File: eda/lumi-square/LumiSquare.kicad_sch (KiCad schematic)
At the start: 70 parts, among them J1 Conn_01x02, J2 Conn_01x02, J3 Conn_01x02, J4 Conn_01x02, J5 USB_C_Receptacle_USB2.0, J6 Conn_01x04, J7 Conn_01x04, J8 Conn_01x04, J9 Conn_01x04, Q1 Q_PMOS_GSD, Q2 Q_PMOS_GSD, Q3 Q_PMOS_GSD, Q4 Q_PMOS_GSD, Q5 MMBT3904, Q6 MMBT3904, Q7 MMBT3904, Q8 MMBT3904, U1 MCP2200-I-SO, U2 ATmega1284-A, U3 ATtiny861A-S, U4 STP16CPC05MTR, U5 TPS3840, U6 TPS3840

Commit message: - Connected power portion of the schmatic - added components to the pcb editor
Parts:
- removed C1, C2, C3, C4: C_Polarized_US, Capacitor_SMD:CP_Elec_5x5.3, symbol Device:C_Polarized_US
- removed C10, C15, C16, C17, C18, C19, C20, C21, C5, C6, C7, C8, C9: C, Capacitor_SMD:C_0805_2012Metric_Pad1.18x1.45mm_HandSolder, symbol Device:C
- removed J1, J2, J3, J4: Conn_01x02, Connector_PinSocket_2.54mm:PinSocket_1x02_P2.54mm_Vertical, symbol Connector_Generic:Conn_01x02
- removed J5: USB_C_Receptacle_USB2.0, Connector_USB:USB_C_Receptacle_G-Switch_GT-USB-7010ASV, symbol Connector:USB_C_Receptacle_USB2.0
- removed Q1, Q2, Q3, Q4: Q_PMOS_GSD, Package_TO_SOT_SMD:SOT-23, symbol Device:Q_PMOS_GSD
- removed Q8: MMBT3904, Package_TO_SOT_SMD:SOT-23, symbol Transistor_BJT:MMBT3904
- removed R1, R10, R11, R12, R13, R14, R15, R16, R17, R18, R19, R2, R20, R21, R22, R23, R24, R25, R3, R4, R5, R6, R7, R8, R9: R, Resistor_SMD:R_0805_2012Metric, symbol Device:R
- removed U1: MCP2200-I-SO, Package_SO:SOIC-20W_7.5x12.8mm_P1.27mm, symbol Interface_USB:MCP2200-I-SO
- removed U2: ATmega1284-A, Package_QFP:TQFP-44_10x10mm_P0.8mm, symbol MCU_Microchip_ATmega:ATmega1284-A
- removed U5, U6: TPS3840, Package_TO_SOT_SMD:SOT-23-5, symbol Power_Supervisor_Custom:TPS3840
- added BT1: 4.2V Lipo, Connector_JST:JST_PH_S2B-PH-SM4-TB_1x02-1MP_P2.00mm_Horizontal, symbol Device:Battery_Cell
- added C1, C2: 4.7uF, Capacitor_SMD:C_0603_1608Metric_Pad1.08x0.95mm_HandSolder, symbol Device:C
- added C10, C8, C9: 100uF, Capacitor_THT:CP_Radial_D6.3mm_P2.50mm, symbol Device:C_Polarized
- added C23234545, C3: 1uF, Capacitor_SMD:C_0603_1608Metric_Pad1.08x0.95mm_HandSolder, symbol Device:C
- added C3245345: 2.2uF, Capacitor_SMD:C_0603_1608Metric_Pad1.08x0.95mm_HandSolder, symbol Device:C
- added C4, C6: 10uF, Capacitor_SMD:C_1206_3216Metric, symbol Device:C_Small
- added C5, C7: 22uF, Capacitor_SMD:C_1206_3216Metric, symbol Device:C_Small
- added D1: LED, LED_SMD:LED_1206_3216Metric, symbol Device:LED
- added D2, D3: 1N5819HW-7-F, Diode_SMD:D_SOD-123, symbol Diode:1N5819WS
- added D4: 1N4148W, Diode_SMD:D_SOD-123, symbol Diode:1N4148W
- added J1: USB_C_Receptacle_USB2.0_14P, Connector_USB:USB_C_Receptacle_G-Switch_GT-USB-7010ASV, symbol Connector:USB_C_Receptacle_USB2.0_14P
- added J6, J7: Conn_01x04, Connector_PinSocket_2.54mm:PinSocket_1x04_P2.54mm_Vertical, symbol Connector_Generic:Conn_01x04
- added L1, L2: 4.7uH, InductorCustom:Bourns SRP30xx, symbol Device:L
- added Q1: IRLML6244, Package_TO_SOT_SMD:SOT-23, symbol Transistor_FET:IRLML6244
- added Q2, Q4: MMBT3904, Package_TO_SOT_SMD:SOT-23, symbol Transistor_BJT:MMBT3904
- added Q3: IRLML2246, Package_TO_SOT_SMD:SOT-23, symbol Transistor_FET:IRLML6401
- added R1, R2: 5.1k, Resistor_SMD:R_0603_1608Metric_Pad0.98x0.95mm_HandSolder, symbol Device:R_US
- added R10, R8: 80k, Resistor_SMD:R_0603_1608Metric, symbol Device:R_Small_US
- added R11: 300, Resistor_SMD:R_0603_1608Metric_Pad0.98x0.95mm_HandSolder, symbol Device:R_US
- added R12: 100k, Resistor_SMD:R_0603_1608Metric_Pad0.98x0.95mm_HandSolder, symbol Device:R_US
- added R13, R3: 10k, Resistor_SMD:R_0603_1608Metric_Pad0.98x0.95mm_HandSolder, symbol Device:R_US
- added R14, R15: 200k, Resistor_SMD:R_0603_1608Metric_Pad0.98x0.95mm_HandSolder, symbol Device:R_US
- added R16, R17, R18, R19: 2.2k, Resistor_SMD:R_0603_1608Metric_Pad0.98x0.95mm_HandSolder, symbol Device:R_US
- added R4: 330, Resistor_SMD:R_0603_1608Metric_Pad0.98x0.95mm_HandSolder, symbol Device:R_US
- added R5: 1.3k, Resistor_SMD:R_0603_1608Metric_Pad0.98x0.95mm_HandSolder, symbol Device:R_Small_US
- added R6: 150k, Resistor_SMD:R_0603_1608Metric_Pad0.98x0.95mm_HandSolder, symbol Device:R_US
- added R7, R9: 720k, Resistor_SMD:R_0603_1608Metric_Pad0.98x0.95mm_HandSolder, symbol Device:R_Small_US
- added SW1: SW_Push, Connector_PinSocket_2.54mm:PinSocket_1x02_P2.54mm_Vertical, symbol Switch:SW_Push
- added U1: MCP73831-2-OT, Package_TO_SOT_SMD:SOT-23-5, symbol Battery_Management:MCP73831-2-OT
- added U2: TPS3840, Package_TO_SOT_SMD:SOT-23-5, symbol Power_Supervisor_Custom:TPS3840
- added U3, U4: TLV61070A, Package_TO_SOT_SMD:SOT-23-6, symbol DCDC-Converter-Boost:TLV61070A
- added U3333333: ATSAMD21J18A-A, Package_QFP:TQFP-64_10x10mm_P0.5mm, symbol MCU_Microchip_SAMD:ATSAMD21J18A-A
- added U8: MIC5225-3.3YM5, Package_TO_SOT_SMD:SOT-23-5, symbol Regulator_Linear:MIC5219-2.5YM5
- C11, C12, C13, C14: value C -> .1uF; footprint Capacitor_SMD:C_0805_2012Metric_Pad1.18x1.45mm_HandSolder -> Capacitor_SMD:C_0603_1608Metric_Pad1.08x0.95mm_HandSolder
- renumbered J6 to J2, J7 to J3, J8 to J4, J9 to J5, U3 to U5, U4 to U6
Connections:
- net 5.3V Out: now reaches C12.1
- net 5.3V Out: now also C11.1, U5.15 (AVCC), U5.5 (VCC), C10.1, C8.1, C9.1, D2.1 (K), D3.1 (K), D4.1 (K), Q3.2 (S), R13.1, R14.1, R15.1
- net GNDREF: now reaches C12.2
- net GNDREF: now also C11.2, C13.2, C14.2, U5.16 (AGND), U5.6 (GND), U6.1 (GND), BT1.2 (-), C1.2, C10.2, C2.2, C23234545.2, C3.2, C3245345.2, C4.1, C5.2, C6.2, C7.2, C8.2, C9.2, J1.A1 (GND), J1.A12 (GND), J1.B1 (GND), J1.B12 (GND), Q1.2 (S), Q2.2 (E), R1.2, R10.2, R12.2, R2.2, R3.2, R5.2, R8.2, SW1.1, U1.2 (V_{SS}), U2.3 (GND), U3.2 (GND), U4.2 (GND), U8.2 (GND)
- net at U6.10 (LED6): now also J3.4 (Pin_4)
- net at U6.11 (LED7): now also J4.2 (Pin_2)
- net at U6.12 (LED8): now also J4.3 (Pin_3)
- net at U6.13 (LED9): now also J4.4 (Pin_4)
- net at U6.14 (LED10): now also J5.2 (Pin_2)
- net at U6.15 (LED11): now also J5.3 (Pin_3)
- net at U6.16 (LED12): now also J5.4 (Pin_4)
- net +3.3V Main: now reaches U6.24 (VDD)
- net +3.3V Main: now also C3245345.1, U8.5 (OUT)
- net at U6.5 (LED1): now also J2.2 (Pin_2)
- net at U6.6 (LED2): now also J2.3 (Pin_3)
- net at U6.7 (LED3): now also J2.4 (Pin_4)
- net at U6.8 (LED4): now also J3.2 (Pin_2)
- net at U6.9 (LED5): now also J3.3 (Pin_3)
- net AREF: now reaches C13.1
- net AREF: now also U5.17 (AREF/PA3)
- net PB7: now reaches C14.1
- net PB7: now also U5.10 (~{RESET}/PB7), D4.2 (A), R15.2
- net at U5.11 (PA7): now also R11.1, R12.1
- net PB6: now reaches U5.9 (PB6)
- net PB6: now also R14.2, SW1.2
- new net: J1.A5 (CC1), R2.1
- new net: Q2.1 (B), R11.2
- new net: Q2.3 (C), Q3.1 (G), R13.2
- new net: L1.2, U3.1 (SW)
- new net: D1.1 (K), U1.1 (STAT)
- new net: R3.1, U1.5 (PROG)
- new net: C7.1, D3.2 (A), R9.1, U4.5 (VOUT)
- new net: R10.1, R9.2, U4.4 (FB)
- new net: L2.2, U4.1 (SW)
- new net: D1.2 (A), R4.2
- new net: Q1.3 (D), R6.2, U2.1 (RESET), U3.3 (EN)
- new net: R7.2, R8.1, U3.4 (FB)
- new net: C5.1, D2.2 (A), R7.1, U3.5 (VOUT)
- new net: C23234545.1, Q3.3 (D), U8.1 (IN), U8.3 (EN)
- new net: U3333333.22 (GND), U3333333.33 (GND), U3333333.47 (GND), U3333333.54 (GND)
- new net: J1.B5 (CC2), R1.1
- new net 4.2V Bat: BT1.1 (+), C2.1, C3.1, C4.2, L1.1, R6.1, U1.3 (V_{BAT}), U2.2 (VDD), U3.6 (VIN)
- new net 5V USB: C1.1, C6.1, J1.A4 (VBUS), J1.A9 (VBUS), J1.B4 (VBUS), J1.B9 (VBUS), L2.1, Q1.1 (G), R4.1, R5.1, U1.4 (V_{DD}), U4.3 (EN), U4.6 (VIN)
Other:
- moved on the sheet: J2, J3, J4, J5, U5, U6

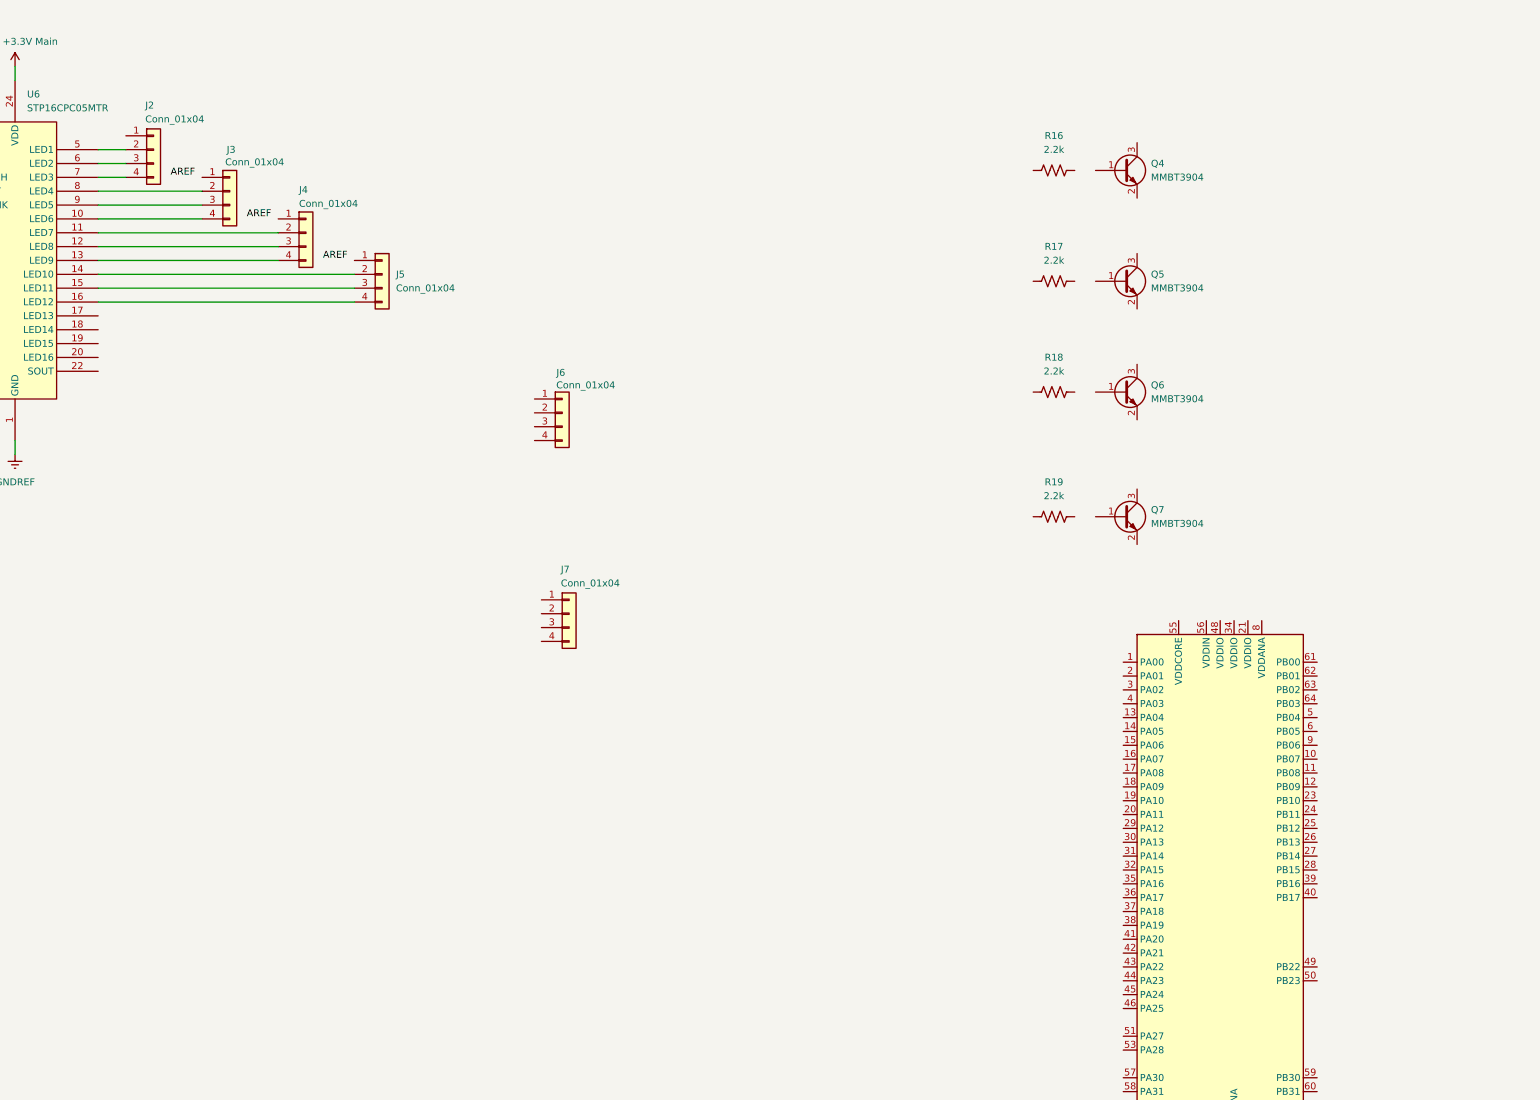
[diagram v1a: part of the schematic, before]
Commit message: - Made updates to LumiSquare pcb and schematic
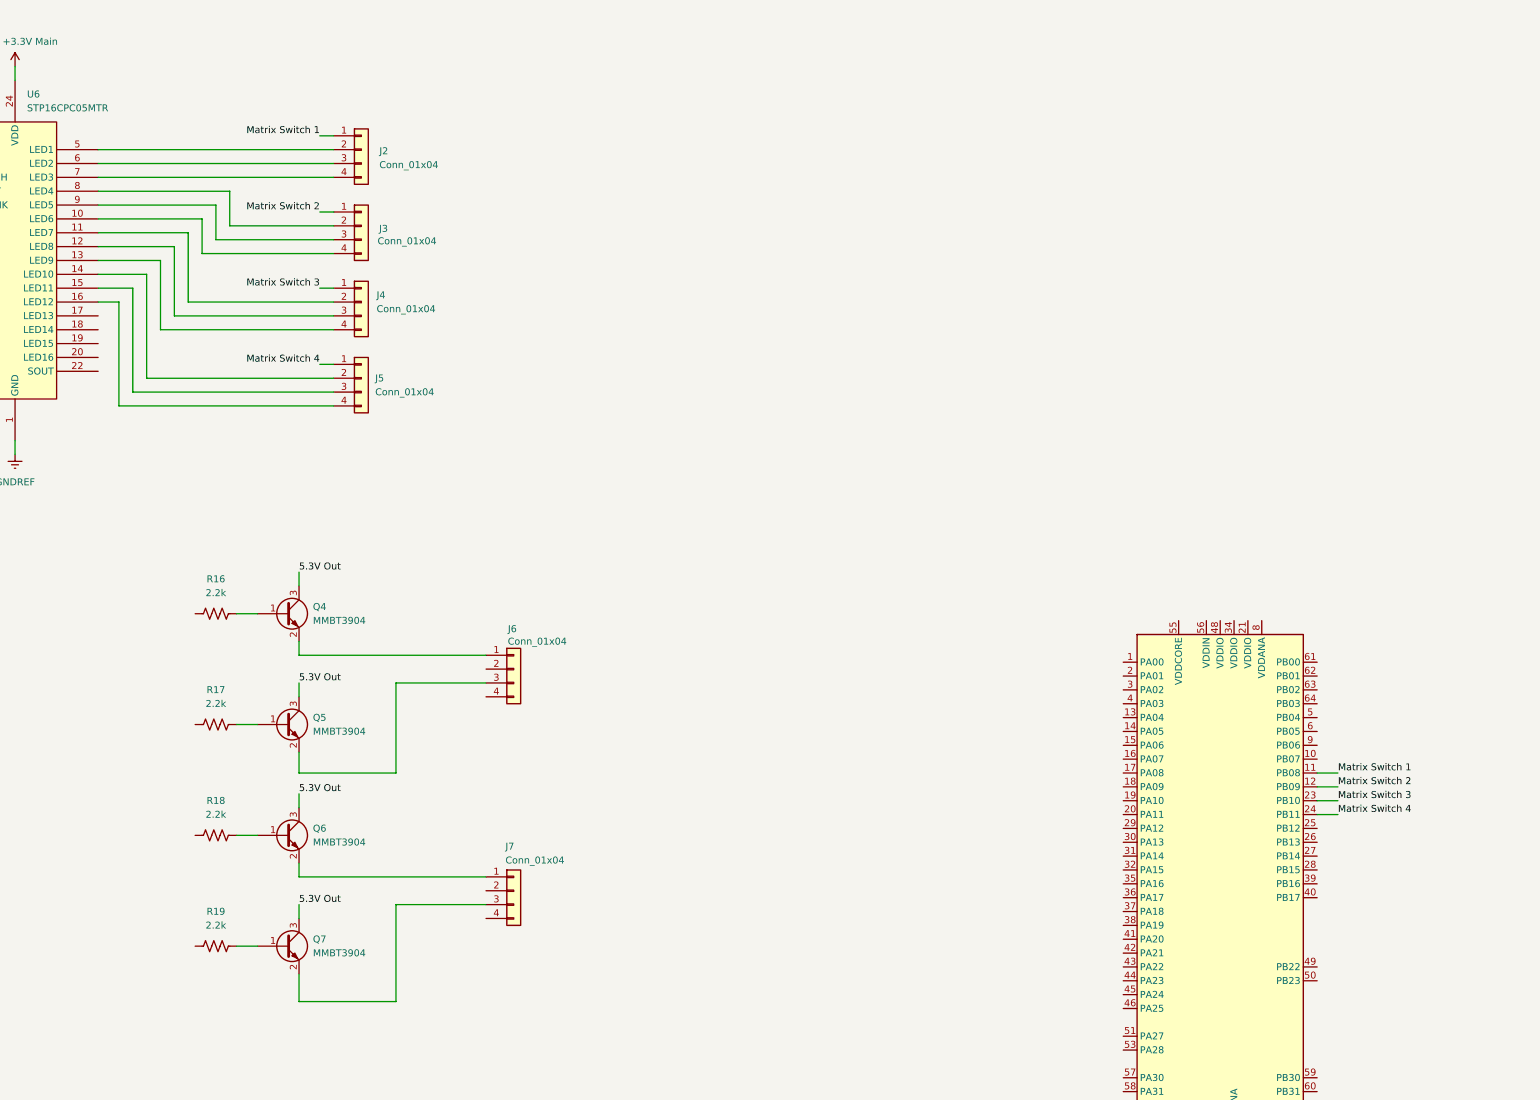
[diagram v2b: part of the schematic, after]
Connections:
- net 5.3V Out: now also Q4.3 (C), Q5.3 (C), Q6.3 (C), Q7.3 (C)
- net Matrix Switch 2: now reaches J3.1 (Pin_1)
- net Matrix Switch 2: now also U3333333.12 (PB09)
- net Matrix Switch 3: now reaches J4.1 (Pin_1)
- net Matrix Switch 3: now also U3333333.23 (PB10)
- net at J7.1 (Pin_1): now also Q6.2 (E)
- net at J7.3 (Pin_3): now also Q7.2 (E)
- net at Q4.1 (B): now also R16.2
- net at Q4.2 (E): now also J6.1 (Pin_1)
- net at Q5.1 (B): now also R17.2
- net at Q5.2 (E): now also J6.3 (Pin_3)
- net at R18.2: now also Q6.1 (B)
- net Matrix Switch 1: now reaches U3333333.11 (PB08)
- net Matrix Switch 1: now also J2.1 (Pin_1)
- net Matrix Switch 4: now reaches U3333333.24 (PB11)
- net Matrix Switch 4: now also J5.1 (Pin_1)
- net at R19.2: now also Q7.1 (B)
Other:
- moved on the sheet: J2, J3, J4, J5, J6, J7, Q4, Q5, Q6, Q7, R16, R17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

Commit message: Adding button matrix kicad project- - Used dma to send audio usart data for samd21
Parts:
- removed C11, C12, C13, C14: .1uF, Capacitor_SMD:C_0603_1608Metric_Pad1.08x0.95mm_HandSolder, symbol Device:C
- removed D4: 1N4148W, Diode_SMD:D_SOD-123, symbol Diode:1N4148W
- removed Q2: MMBT3904, Package_TO_SOT_SMD:SOT-23, symbol Transistor_BJT:MMBT3904
- removed R11: 300, Resistor_SMD:R_0603_1608Metric_Pad0.98x0.95mm_HandSolder, symbol Device:R_US
- removed R12: 100k, Resistor_SMD:R_0603_1608Metric_Pad0.98x0.95mm_HandSolder, symbol Device:R_US
- removed R14, R15: 200k, Resistor_SMD:R_0603_1608Metric_Pad0.98x0.95mm_HandSolder, symbol Device:R_US
- removed SW1: SW_Push, Connector_PinSocket_2.54mm:PinSocket_1x02_P2.54mm_Vertical, symbol Switch:SW_Push
- removed U5: ATtiny861A-S, Package_SO:SOIC-20W_7.5x12.8mm_P1.27mm, symbol MCU_Microchip_ATtiny:ATtiny861A-S

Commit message: - uploading kicad pcb changes
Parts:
- removed J2, J3, J4, J5, J6, J7: Conn_01x04, Connector_PinSocket_2.54mm:PinSocket_1x04_P2.54mm_Vertical, symbol Connector_Generic:Conn_01x04
- added BZ1: Buzzer, symbol Device:Buzzer
- added C11: .001uF, Capacitor_SMD:C_0603_1608Metric_Pad1.08x0.95mm_HandSolder, symbol Device:C
- added C12: .01uF, Capacitor_SMD:C_0603_1608Metric_Pad1.08x0.95mm_HandSolder, symbol Device:C
- added C13, C14, C15: 1uF, Capacitor_THT:CP_Radial_D6.3mm_P2.50mm, symbol Device:C_Polarized
- added C16, C17, C18, C19, C20, C21: .1uF, Capacitor_SMD:C_1206_3216Metric, symbol Device:C_Small
- added D4: 1N4148W, Diode_SMD:D_SOD-123, symbol Diode:1N4148W
- added D5: LED, LED_SMD:LED_1206_3216Metric, symbol Device:LED
- added J2, J3: Conn_01x12, Connector_PinSocket_2.54mm:PinSocket_1x12_P2.54mm_Vertical, symbol Connector_Generic:Conn_01x12
- added J4: Conn_ARM_JTAG_SWD_10, symbol Connector:Conn_ARM_JTAG_SWD_10
- added J5, J6: Conn_01x08, Connector_PinSocket_2.54mm:PinSocket_1x08_P2.54mm_Vertical, symbol Connector_Generic:Conn_01x08
- added Q10, Q2: IRLML2246, Package_TO_SOT_SMD:SOT-23, symbol Transistor_FET:IRLML6401
- added Q8, Q9: MMBT3904, Package_TO_SOT_SMD:SOT-23, symbol Transistor_BJT:MMBT3904
- added R11: 220k, Resistor_SMD:R_0603_1608Metric_Pad0.98x0.95mm_HandSolder, symbol Device:R_Small_US
- added R12: 1k, Resistor_SMD:R_0603_1608Metric_Pad0.98x0.95mm_HandSolder, symbol Device:R_Small_US
- added R14, R15, R20: 15k, Resistor_SMD:R_0603_1608Metric_Pad0.98x0.95mm_HandSolder, symbol Device:R_US
- added R21: 10k, Resistor_SMD:R_0603_1608Metric_Pad0.98x0.95mm_HandSolder, symbol Device:R_US
- added R22: 2.2k, Resistor_SMD:R_0603_1608Metric_Pad0.98x0.95mm_HandSolder, symbol Device:R_US
- added R23: 330, Resistor_SMD:R_0603_1608Metric_Pad0.98x0.95mm_HandSolder, symbol Device:R_US
- added R24, R25: 1.3k, Resistor_SMD:R_0603_1608Metric_Pad0.98x0.95mm_HandSolder, symbol Device:R_US
- added R26: 33k, Resistor_SMD:R_0603_1608Metric_Pad0.98x0.95mm_HandSolder, symbol Device:R_US
- added R27: 41k, Resistor_SMD:R_0603_1608Metric_Pad0.98x0.95mm_HandSolder, symbol Device:R_US
- added R28: 100k, Resistor_SMD:R_0603_1608Metric_Pad0.98x0.95mm_HandSolder, symbol Device:R_US
- added SW1: SW_SPST, symbol Switch:SW_SPST
- added SW2, SW3, SW4, SW5: SW_Push, symbol Switch:SW_Push
- R13: value 10k -> 100k
- renumbered U3333333 to U5
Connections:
- net +3.3V Main: now also U5.21 (VDDIO), U5.34 (VDDIO), U5.48 (VDDIO), U5.56 (VDDIN), U5.8 (VDDANA), BZ1.1 (+), C11.1, C12.1, C17.1, C18.1, C19.1, C20.1, C21.1, D4.1 (K), J4.1 (VTref), J5.1 (Pin_1), R21.1, R23.2, R24.1
- net 4.2V Bat: now also Q2.2 (S); no longer C3.1, C4.2, L1.1, R6.1, U2.2 (VDD), U3.6 (VIN)
- net 5V USB: now also Q10.2 (S), Q2.1 (G), R11.1, R28.1
- net GNDREF: now also U5.22 (GND), U5.33 (GND), U5.47 (GND), U5.54 (GND), U5.7 (GNDANA), U6.21 (BLANK), C11.2, C12.2, C13.2, C14.2, C15.2, C16.2, C17.2, C18.2, C19.2, C20.2, C21.2, D5.2 (A), J4.3 (GND), J4.5 (GND), J5.7 (Pin_7), Q8.2 (E), Q9.2 (E), R11.2, R12.2, R25.2, R27.2, SW1.1 (A), SW2.1, SW3.1, SW4.1, SW5.1
- net at U6.10 (LED6): now also J2.6 (Pin_6)
- net at U6.11 (LED7): now also J2.7 (Pin_7)
- net at U6.12 (LED8): now also J2.8 (Pin_8)
- net at U6.13 (LED9): now also J2.9 (Pin_9)
- net at U6.14 (LED10): now also J2.10 (Pin_10)
- net at U6.15 (LED11): now also J2.11 (Pin_11)
- net at U6.16 (LED12): now also J2.12 (Pin_12)
- net SPI Dout: now reaches U6.2 (SIN)
- net SPI Dout: now also U5.25 (PB12)
- net at U6.23 (RSET): now also R12.1
- net SPI CLK: now reaches U6.3 (CLK)
- net SPI CLK: now also U5.26 (PB13)
- net SPI Latch: now reaches U6.4 (LATCH)
- net SPI Latch: now also U5.27 (PB14)
- net at U6.5 (LED1): now also J2.1 (Pin_1)
- net at U6.6 (LED2): now also J2.2 (Pin_2)
- net at U6.7 (LED3): now also J2.3 (Pin_3)
- net at U6.8 (LED4): now also J2.4 (Pin_4)
- net at U6.9 (LED5): now also J2.5 (Pin_5)
- net at Q6.2 (E): now also J3.11 (Pin_11)
- net at Q7.2 (E): now also J3.12 (Pin_12)
- net at Q4.2 (E): now also J3.9 (Pin_9)
- net at Q5.2 (E): now also J3.10 (Pin_10)
- net LED Col 3: now reaches R18.1
- net LED Col 3: now also U5.63 (PB02)
- net Col/Output 4: now reaches U5.10 (PB07)
- net Col/Output 4: now also J3.8 (Pin_8)
- net PA14 USB VBUS: now reaches U5.31 (PA14)
- net PA14 USB VBUS: now also R26.2, R27.1
- net Previous Btn: now reaches U5.39 (PB16)
- net Previous Btn: now also C13.1, R14.2
- net Next Btn: now reaches U5.40 (PB17)
- net Next Btn: now also C14.1, R15.2
- net MCU TX: now reaches U5.41 (PA20)
- net MCU TX: now also J5.2 (Pin_2)
- net MCU RX: now reaches U5.42 (PA21)
- net MCU RX: now also J5.3 (Pin_3)
- net Difficulty Btn: now reaches U5.49 (PB22)
- net Difficulty Btn: now also C15.1, R20.2
- net Col/Output 1: now reaches U5.5 (PB04)
- net Col/Output 1: now also J3.5 (Pin_5)
- net Buzzer PWM: now reaches U5.50 (PB23)
- net Buzzer PWM: now also R22.1
- net Reset Pin: now reaches U5.52 (~{RESET})
- net Reset Pin: now also J4.10 (~{RESET}), R21.2, SW5.2
- net VDD CORE: now reaches U5.55 (VDDCORE)
- net VDD CORE: now also C16.1
- net SWCLK: now reaches U5.57 (PA30)
- net SWCLK: now also J4.4 (SWCLK/TCK)
- net SWDIO: now reaches U5.58 (PA31)
- net SWDIO: now also J4.2 (SWDIO/TMS)
- net Col/Output 2: now reaches U5.6 (PB05)
- net Col/Output 2: now also J3.6 (Pin_6)
- net LED Col 1: now reaches U5.61 (PB00)
- net LED Col 1: now also R16.1
- net LED Col 2: now reaches U5.62 (PB01)
- net LED Col 2: now also R17.1
- net LED Col 4: now reaches U5.64 (PB03)
- net LED Col 4: now also R19.1
- net Col/Output 3: now reaches U5.9 (PB06)
- net Col/Output 3: now also J3.7 (Pin_7)
- net at Q3.1 (G), R13.2: now also SW1.2 (B)
- net Matrix Switch 1 renamed Row/Input 1
- net Row/Input 1: now also J3.1 (Pin_1)
- net Matrix Switch 2 renamed Row/Input 2
- net Row/Input 2: now also J3.2 (Pin_2)
- net Matrix Switch 3 renamed Row/Input 3
- net Row/Input 3: now also J3.3 (Pin_3)
- net Matrix Switch 4 renamed Row/Input 4
- net Row/Input 4: now also J3.4 (Pin_4)
- new net: C3.1, C4.2, L1.1, Q2.3 (D), R6.1, U2.2 (VDD), U3.6 (VIN)
- new net: BZ1.2 (-), D4.2 (A), Q8.3 (C)
- new net: Q9.1 (B), R24.2, R25.1
- new net: Q10.1 (G), Q9.3 (C), R28.2
- new net: Q10.3 (D), R26.1
- new net: R15.1, SW3.2
- new net: Q8.1 (B), R22.2
- new net: R14.1, SW2.2
- new net: D5.1 (K), R23.1
- new net: R20.1, SW4.2
- new net Speaker+: J5.6 (Pin_6)
- new net Speaker-: J5.8 (Pin_8)
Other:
- note added: "DF Player"
- note added: "Difficulty Button"
- note added: "JTAG"
- note added: "LED Button Matrix"
- note added: "Next Button"
- note added: "Power Path Management & Boost Conversion"
- note added: "Previous Button"
- note added: "Reset Button"
- note added: "SAMD21J18A"
- note added: "System Power Switch & 3.3V Regulation"
- note added: "Tone Buzzer"
- note added: "USB & LiPo Charger"
- note added: "VDDIO/VDDCORE Caps"
- moved on the sheet: BT1, C1, C10, C2, C23234545, C3, C3245345, C4, C5, C6, C7, C8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
